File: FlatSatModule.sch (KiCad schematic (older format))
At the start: 13 parts, among them J1 DB26_Male_HighDensity_Mountin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, J2 Micro_SD_Card_Det, J3 HEADER_13x2

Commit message: Add X logo, reset version to 1.0 and move microSD label
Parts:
- added G1: LOGO, x-logo:X-LOGO, symbol x-logo:LOGO
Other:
- note added: "1.0"
- note removed: "1.2"
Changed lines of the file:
@@
 $EndBitmap
 Text Notes 15475 11050 0    50   ~ 0
-1.2
+1.0
 Wire Wire Line
 	4500 7300 5000 7300
@@
 Wire Wire Line
 	9125 10475 9125 10375
+$Comp
+L x-logo:LOGO G1
+U 1 1 5F108FC6
+P 10975 10350
+F 0 "G1" H 10975 9711 60  0001 C CNN
+F 1 "LOGO" H 10975 10989 60  0001 C CNN
+F 2 "x-logo:X-LOGO" H 10975 10350 50  0001 C CNN
+F 3 "" H 10975 10350 50  0001 C CNN
+	1    10975 10350
+	1    0    0    -1
+$EndComp
 $EndSCHEMATC

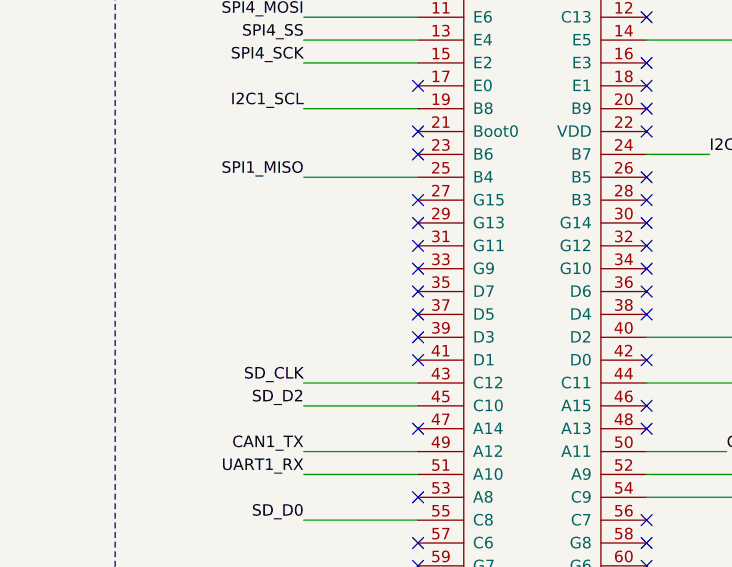
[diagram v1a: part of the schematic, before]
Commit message: wire sd_det to stm32 and correct stm32 footprint
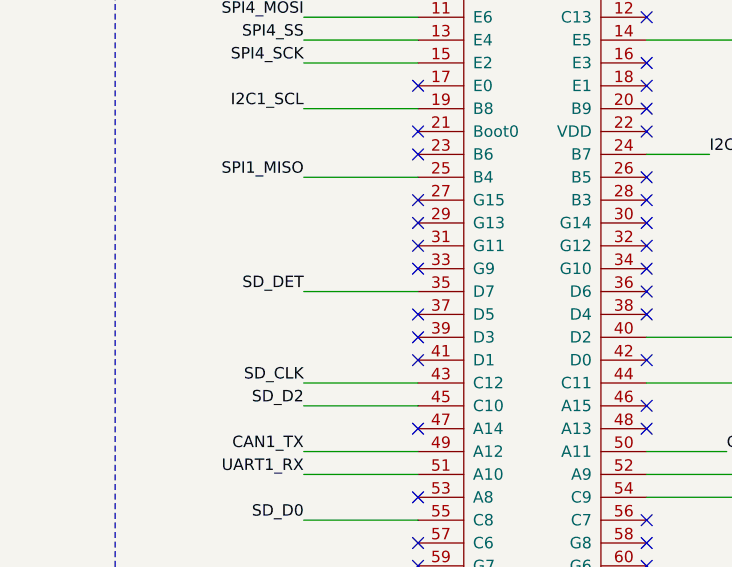
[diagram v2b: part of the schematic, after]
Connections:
- wire segments 92 -> 93
- no-connect marks 104 -> 103
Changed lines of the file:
@@
 UART2_RX
 NoConn ~ 2425 7375
-NoConn ~ 2425 7475
 NoConn ~ 2425 7575
 NoConn ~ 2425 7675
@@
 NoConn ~ 2425 8775
 NoConn ~ 2425 8875
-NoConn ~ 2425 8975
 NoConn ~ 2425 9075
 NoConn ~ 2425 9175
@@
 	1    0    0    -1
 $EndComp
+Wire Wire Line
+	1925 8975 2425 8975
+Text Label 1925 8975 2    50   ~ 0
+SD_DET
+NoConn ~ 2425 7475
 $EndSCHEMATC

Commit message: Added pull down resistor for SD card detect and few track clean.
Signed-off-by: Alexis Jeandet <alexis.jeandet@member.fsf.org>
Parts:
- added R101: R, Resistor_SMD:R_0603_1608Metric_Pad1.05x0.95mm_HandSolder, symbol Device:R
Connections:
- wire segments 93 -> 99
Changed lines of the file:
@@
 	13550 8475 14000 8475
 Wire Wire Line
-	13525 9100 14025 9100
+	13525 9100 13750 9100
 Wire Wire Line
 	12300 8475 12650 8475
@@
 SD_DET
 Wire Wire Line
-	12325 9100 12675 9100
+	12325 9100 12500 9100
 $Comp
 L stm32:STM32F429i-Discovery stm32101
@@
 SD_DET
 NoConn ~ 2425 7475
+$Comp
+L Device:R R101
+U 1 1 5F112142
+P 13375 9450
+F 0 "R101" V 13168 9450 50  0000 C CNN
+F 1 "R" V 13259 9450 50  0000 C CNN
+F 2 "Resistor_SMD:R_0603_1608Metric_Pad1.05x0.95mm_HandSolder" V 13305 9450 50  0001 C CNN
+F 3 "~" H 13375 9450 50  0001 C CNN
+	1    13375 9450
+	0    -1   -1   0
+$EndComp
+Wire Wire Line
+	13525 9450 13750 9450
+Wire Wire Line
+	13750 9450 13750 9100
+Connection ~ 13750 9100
+Wire Wire Line
+	13750 9100 14025 9100
+Wire Wire Line
+	13225 9450 12500 9450
+Wire Wire Line
+	12500 9450 12500 9100
+Connection ~ 12500 9100
+Wire Wire Line
+	12500 9100 12675 9100
 $EndSCHEMATC
